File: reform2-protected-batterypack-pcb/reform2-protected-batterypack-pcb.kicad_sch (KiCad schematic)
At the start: 38 parts, among them J1 Conn_01x05_Female, Q1 PMV50ENEAR, Q2 PMV50ENEAR, Q3 PMV50ENEAR, Q4 PMV50ENEAR, Q5 PMV50ENEAR, Q6 PMV50ENEAR, Q7 PMV50ENEAR, Q8 PMV50ENEAR, U1 KEYSTONE_54, U2 KEYSTONE_54, U3 KEYSTONE_54, U4 KEYSTONE_54, U5 R5617x, U6 R5617x, U7 R5617x, U8 R5617x

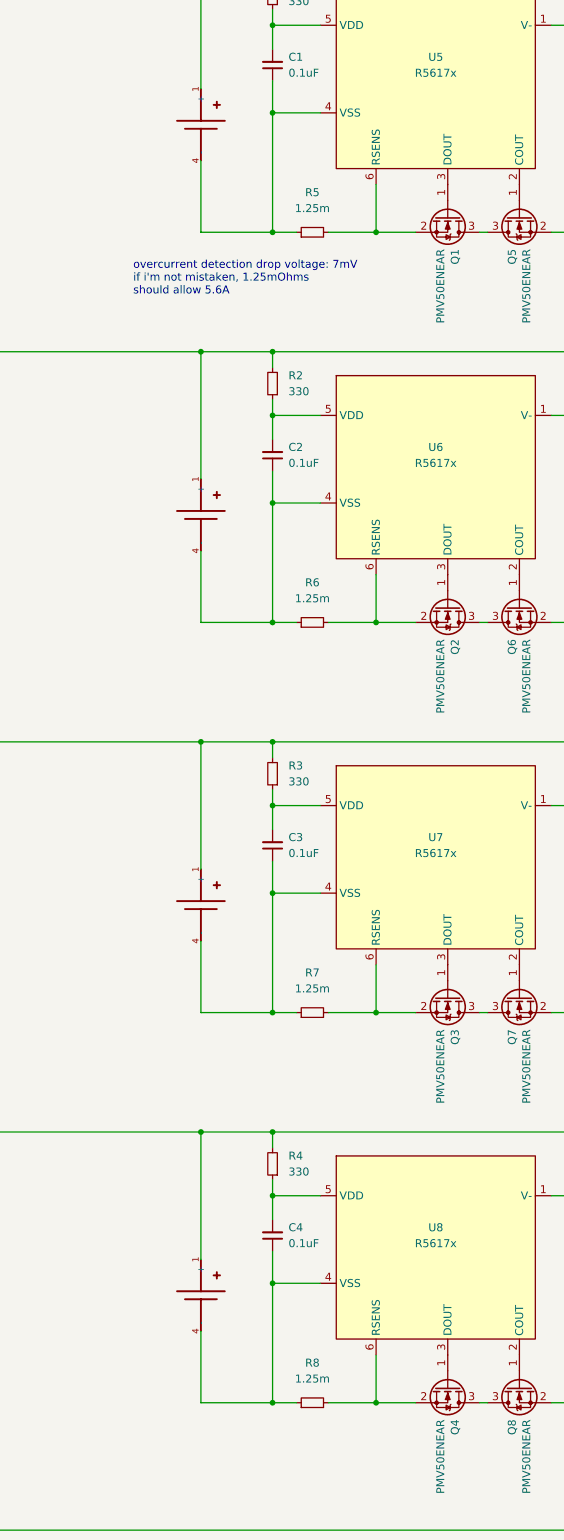
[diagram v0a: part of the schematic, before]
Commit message: protected battery pack: add release candidate
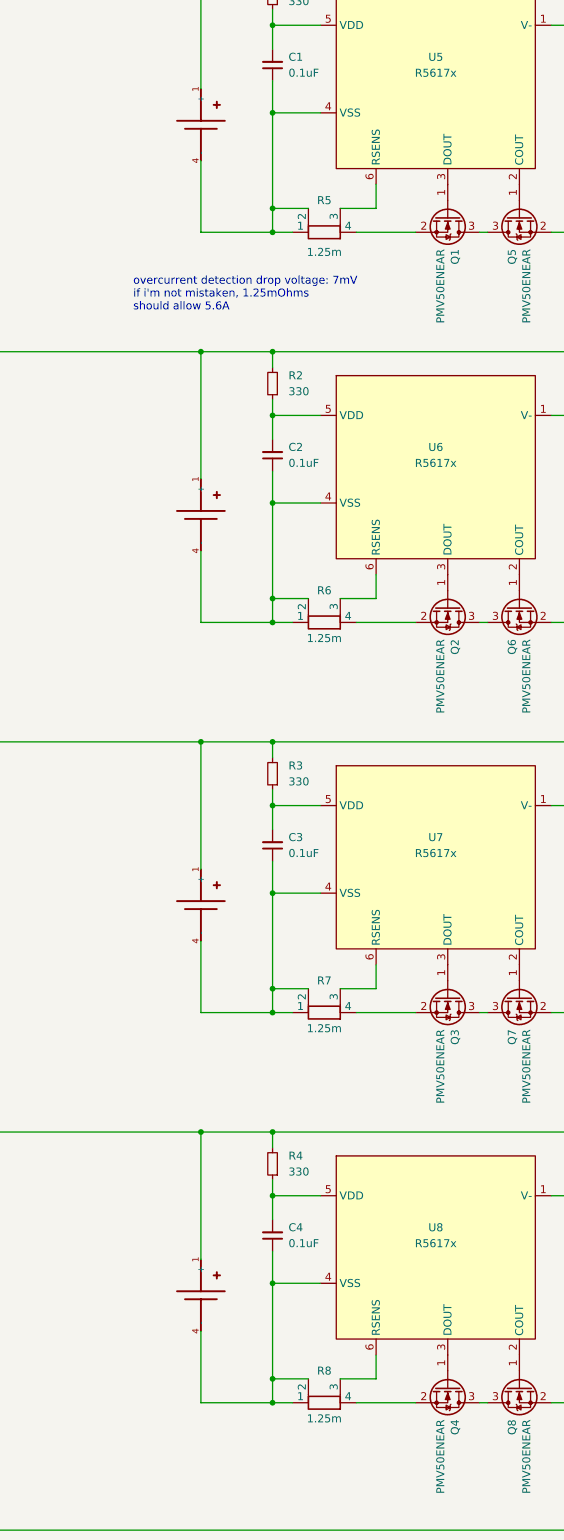
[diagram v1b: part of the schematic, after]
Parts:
- R5, R6, R7, R8: footprint Resistor_SMD:R_0805_2012Metric -> footprints:R_1206_3216Metric_Kelvin; symbol Device:R_Small -> Device:R_Shunt
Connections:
- net at C1.1, R5.1, U1.4 (-)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: now also R5.2
- net at C2.1, R6.1, U2.4 (-)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: now also R6.2
- net at C3.1, R7.1, U3.4 (-)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: now also R7.2
- net at C4.1, R8.1, U4.4 (-)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: now also R8.2
- new net: Q4.2 (S), R8.4
- new net: Q2.2 (S), R6.4
- new net: R5.3, U5.6 (RSENS)
- new net: R7.3, U7.6 (RSENS)
- new net: Q3.2 (S), R7.4
- new net: R6.3, U6.6 (RSENS)
- new net: Q1.2 (S), R5.4
- new net: R8.3, U8.6 (RSENS)
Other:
- company: (none) -> MNT Research GmbH
- title: (none) -> MNT Reform Protected Battery Pack
